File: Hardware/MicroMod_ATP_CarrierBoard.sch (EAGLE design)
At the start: 65 parts, among them J19 QWIIC_RIGHT_ANGLE, J2 JTAG, J20 QWIIC_RIGHT_ANGLE, J21 1X04_SMD_STRAIGHT_COMBO, J4 USB_A_SMT_FEMALE, J6 MICROMOD-2222-C, J8 1X04_SMD_STRAIGHT_COMBO, U5 AP7361C-33

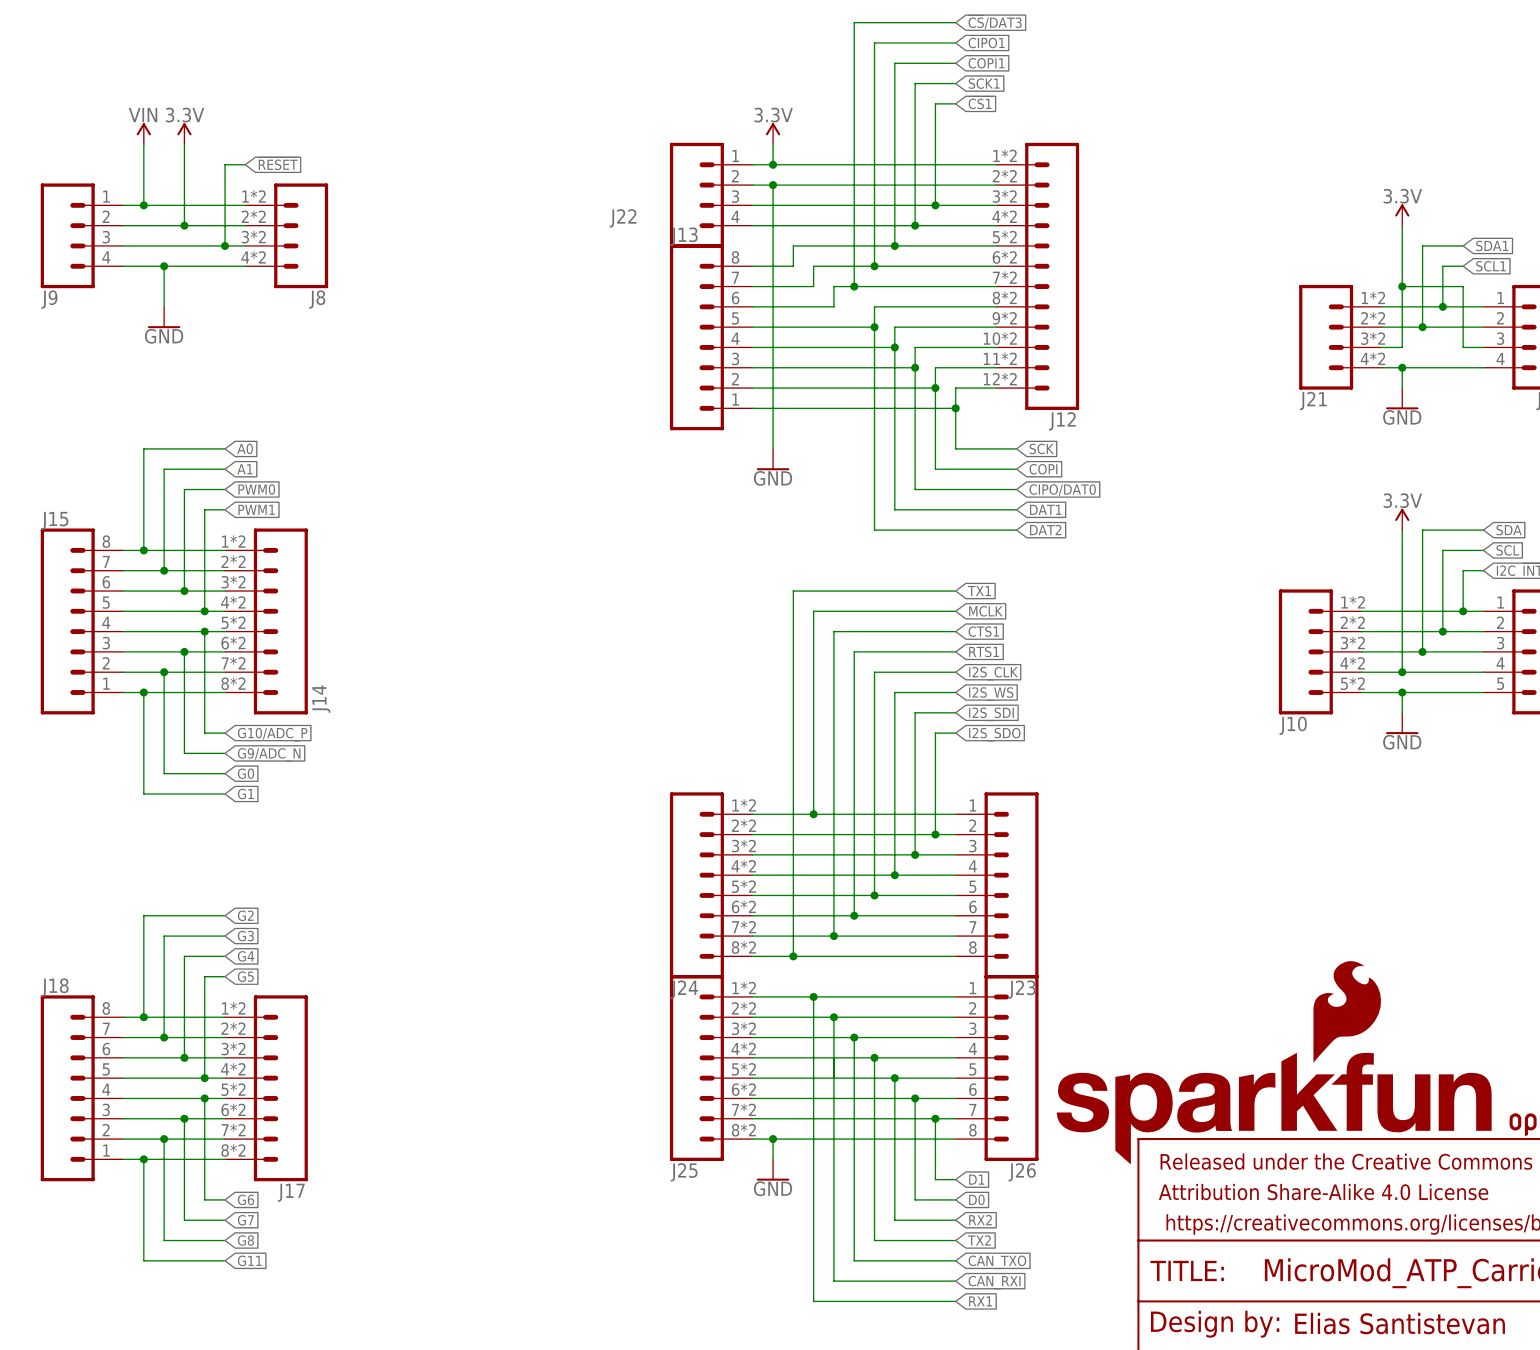
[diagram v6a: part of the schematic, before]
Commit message: Replaces all connectors with their updated version
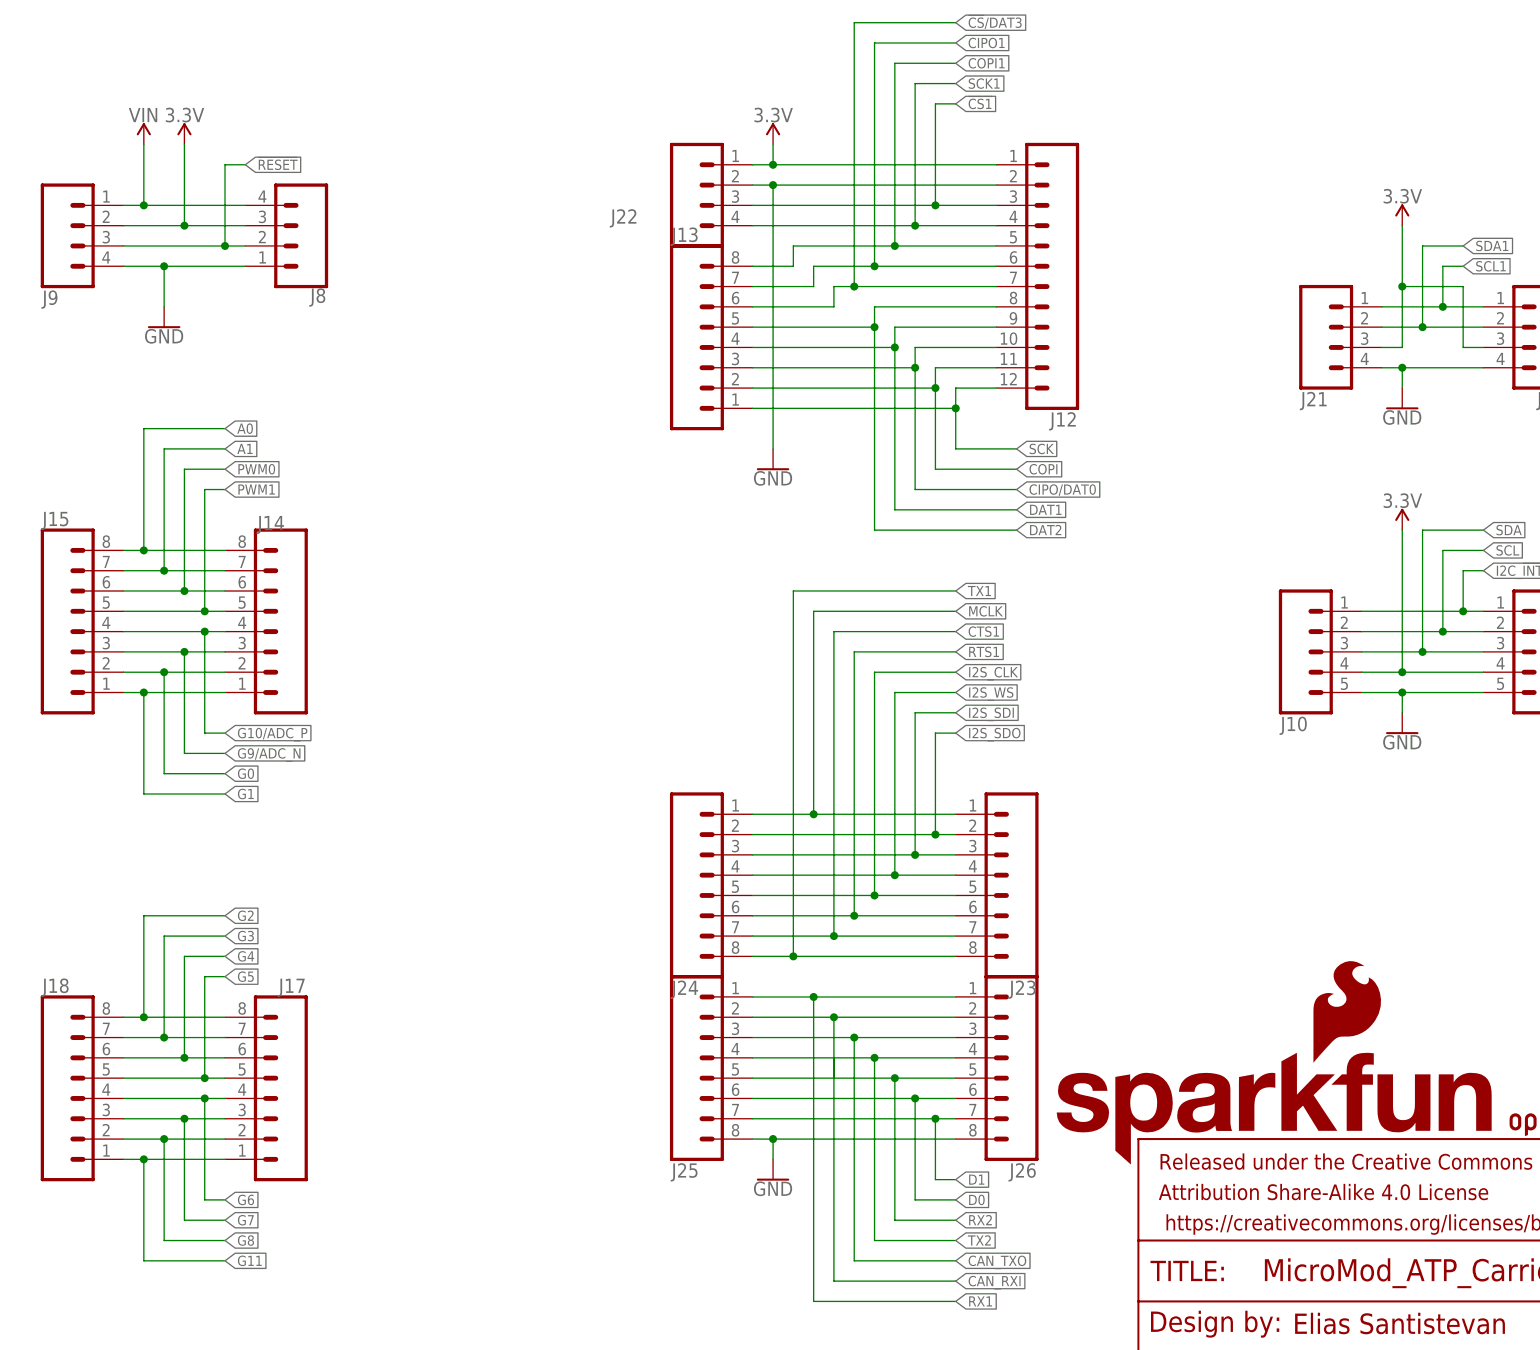
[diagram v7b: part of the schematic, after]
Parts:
- J24: device SparkFun-Connectors:CONN_08SMD-COMBO-FEMALE -> testing_header_lib:CONN_08SMD-COMBO-FEMALE
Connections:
- removed net !RESET!: J8.3, J9.3
- net !RESET: now also J8.2, J9.3
- net 3.3V: now also J8.3; no longer J8.2
- net A0: now also J14.8; no longer J14.1
- net A1: now also J14.7; no longer J14.2
- net G0: now also J14.2; no longer J14.7
- net G1: now also J14.1; no longer J14.8
- net G10/ADC_P: now also J14.4; no longer J14.5
- net G11: now also J17.1; no longer J17.8
- net G2: now also J17.8; no longer J17.1
- net G3: now also J17.7; no longer J17.2
- net G4: now also J17.6; no longer J17.3
- net G5: now also J17.5; no longer J17.4
- net G6: now also J17.4; no longer J17.5
- net G7: now also J17.3; no longer J17.6
- net G8: now also J17.2; no longer J17.7
- net G9/ADC_N: now also J14.3; no longer J14.6
- net GND: now also J8.1; no longer J8.4
- net PWM0: now also J14.6; no longer J14.3
- net PWM1: now also J14.5; no longer J14.4
- net VIN: now also J8.4; no longer J8.1
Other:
- moved on the sheet: J10, J12, J14, J17, J21, J24, J25, J8

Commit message: Swaps one 8 pin header in the test lib to on from the main Sparkfun lib
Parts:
- J24: device testing_header_lib:CONN_08SMD-COMBO-FEMALE -> SparkFun-Connectors:CONN_08SMD-COMBO-FEMALE
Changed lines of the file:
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@@
 <part name="GND18" library="SparkFun-PowerSymbols" deviceset="GND" device=""/>
 <part name="SUPPLY14" library="SparkFun-PowerSymbols" deviceset="3.3V" device=""/>
-<part name="J24" library="testing_header_lib" deviceset="CONN_08" device="SMD-COMBO-FEMALE"/>
+<part name="J24" library="SparkFun-Connectors" deviceset="CONN_08" device="SMD-COMBO-FEMALE"/>
 <part name="J25" library="SparkFun-Connectors" deviceset="CONN_08" device="SMD-COMBO-FEMALE"/>
 <part name="GND4" library="SparkFun-PowerSymbols" deviceset="GND" device=""/>
